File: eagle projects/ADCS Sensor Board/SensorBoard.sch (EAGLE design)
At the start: 88 parts, among them J5 HDR_10_EZFET_DEBUGGER, J6 MTI-1_8428-11B1-RK-TP, Q1 BC850SMD, Q2 IRF7507TRPBF, U1 MSP430F5529IPN, U2 LMV321, U3 ADS7841E_2K5, U4 LMV321, U5 LM20BIM7X_NOPB, U6 LMV321, Y1 32.768kHz, Y2 CSTCR4M00G15L99

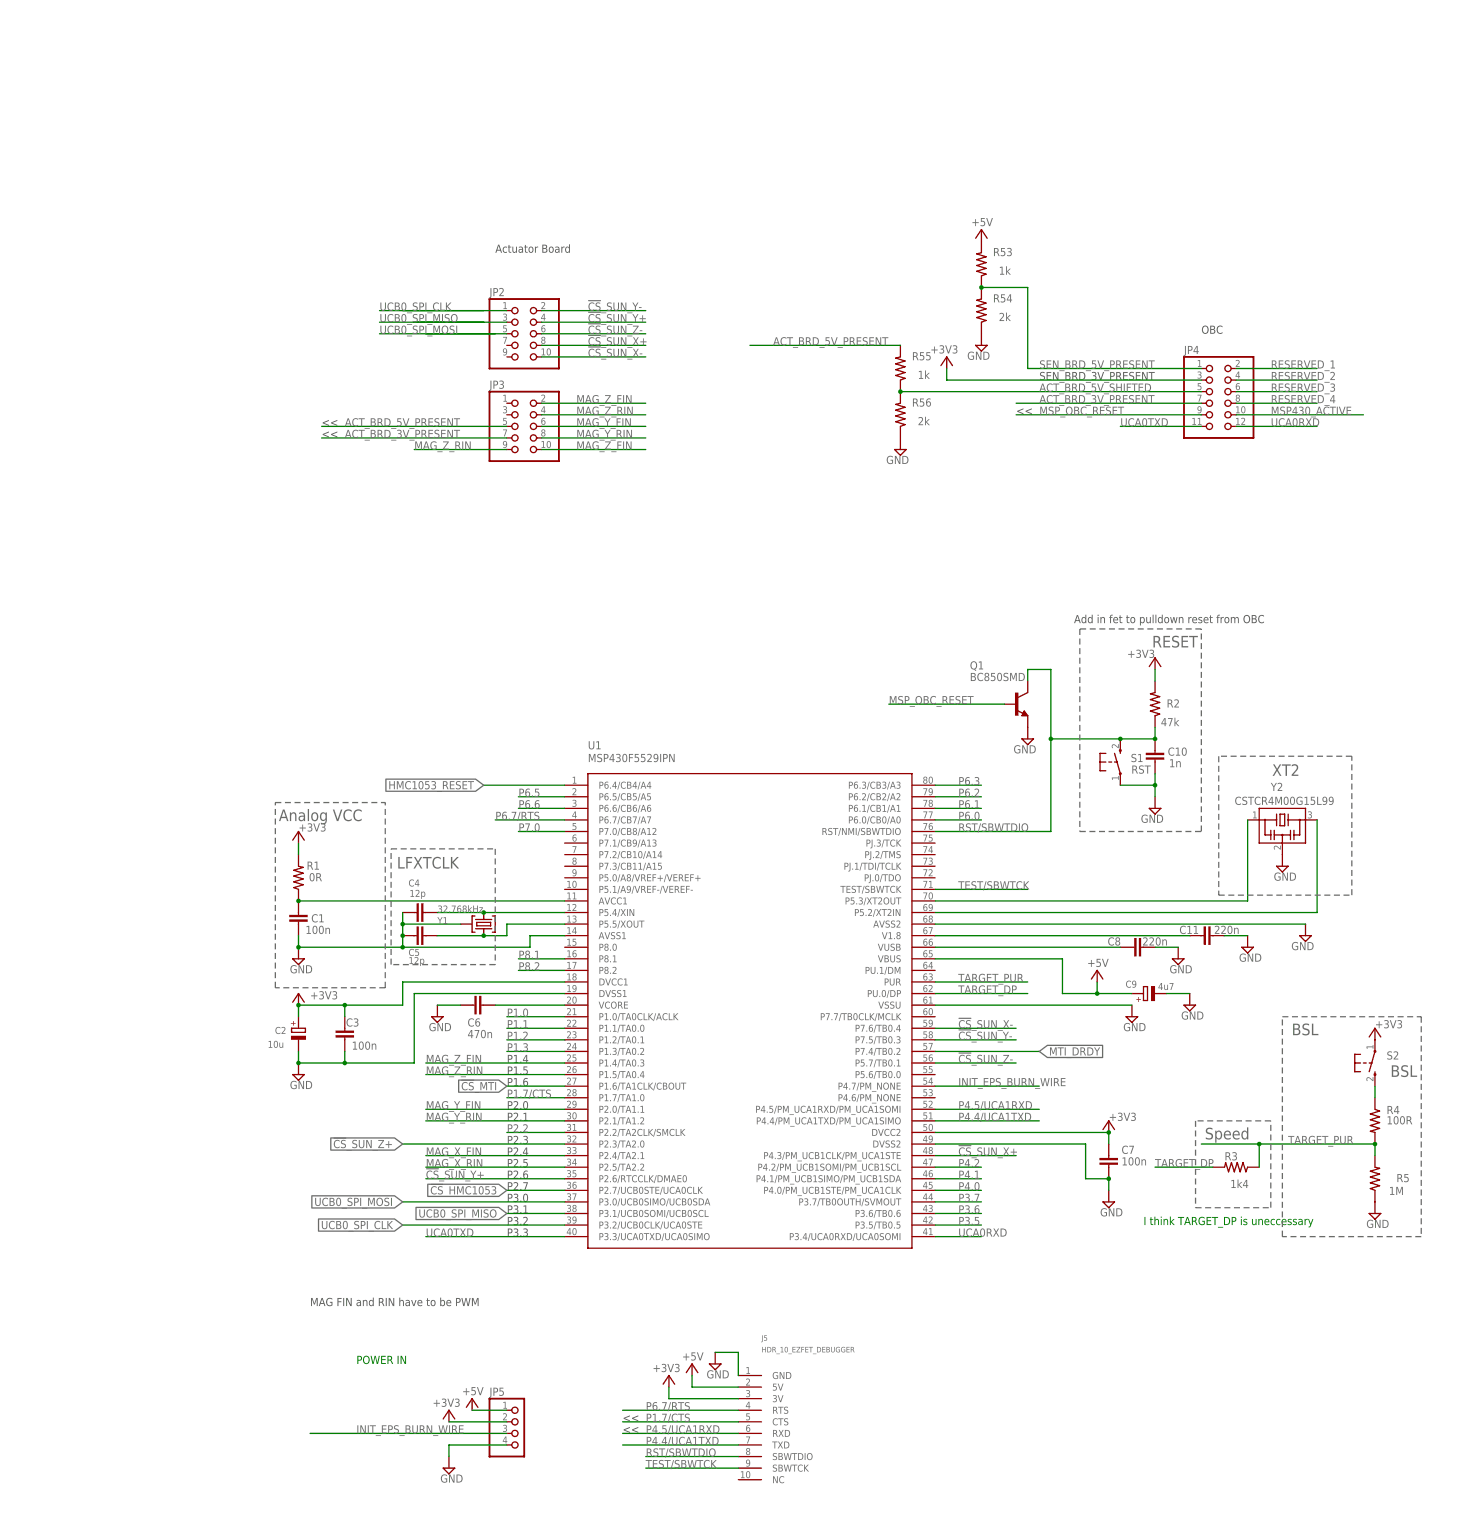
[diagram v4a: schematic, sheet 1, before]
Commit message: removed unused usb stuff from msp430
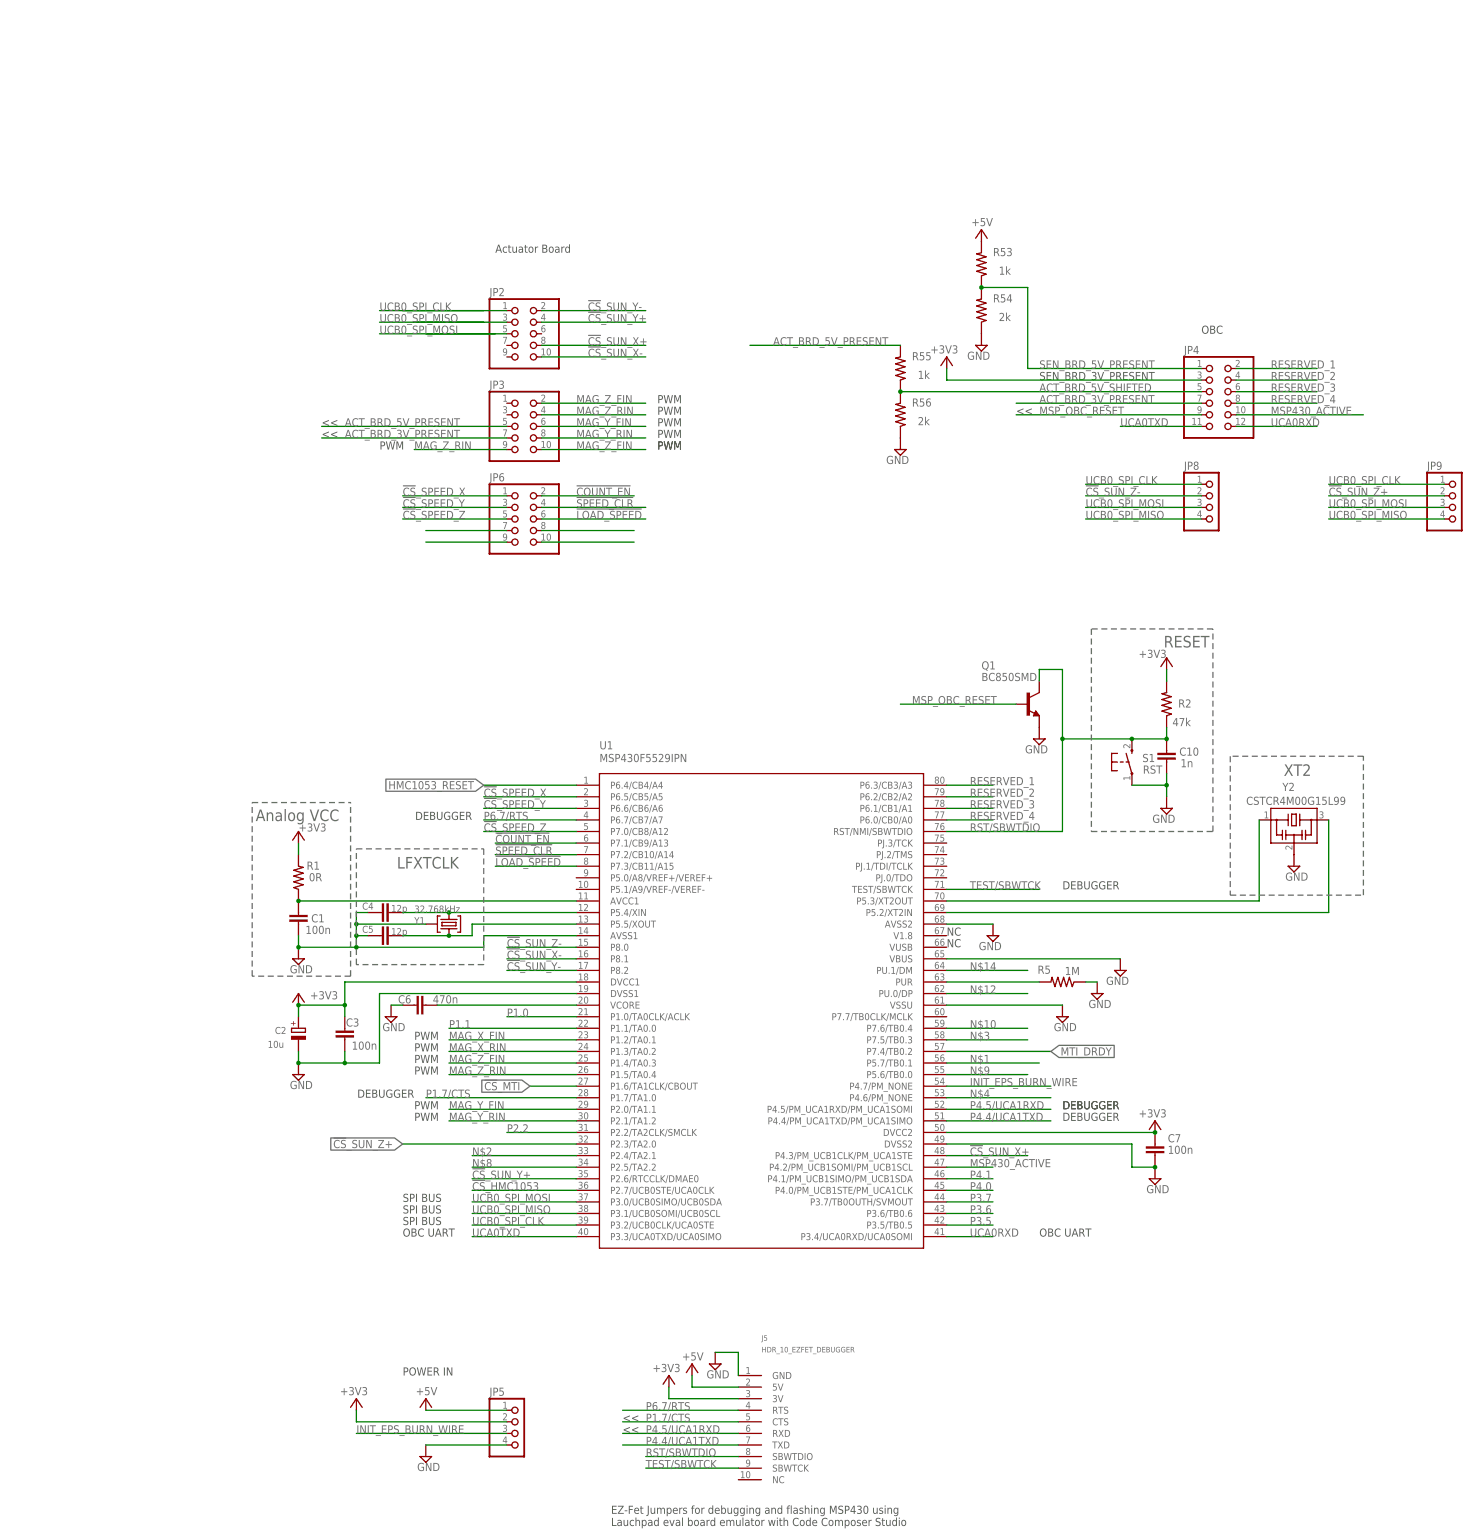
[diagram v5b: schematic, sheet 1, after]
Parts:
- removed C11, C8: 220n, rcl:C-EUC0402
- removed C9: 4u7, rcl:CPOL-EUA/3216-18R
- removed R3: 1k4, rcl:R-US_R0402
- removed R4: 100R, rcl:R-US_R0402
- removed S2: BSL, electricalmeter:PB
- added JP6: (no value), pinhead:PINHD-2X5
- added JP7: (no value), pinhead:PINHD-1X7
- added JP8, JP9: (no value), pinhead:PINHD-1X4
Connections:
- removed net N$17: A3.+5V
- removed net P1.2: U1.P1.2/TA0.1
- removed net P1.3: U1.P1.3/TA0.2
- removed net P4.2: U1.P4.2/PM_UCB1SOMI/PM_UCB1SCL
- removed net P6.0: U1.P6.0/CB0/A0
- removed net P6.1: U1.P6.1/CB1/A1
- removed net P6.2: U1.P6.2/CB2/A2
- removed net P6.3: U1.P6.3/CB3/A3
- removed net P6.5: U1.P6.5/CB5/A5
- removed net P6.6: U1.P6.6/CB6/A6
- removed net P7.0: U1.P7.0/CB8/A12
- removed net P8.1: U1.P8.1
- removed net P8.2: U1.P8.2
- removed net TARGET_DP: R3.2, U1.PU.0/DP
- removed net TARGET_VUSB1: C8.1, U1.VUSB
- removed net V1: C11.1, U1.V1.8
- new net !COUNT_EN: JP6.2, U1.P7.1/CB9/A13
- new net !CS!_SPEED_X: JP6.1, U1.P6.5/CB5/A5
- new net !CS!_SPEED_Y: JP6.3, U1.P6.6/CB6/A6
- new net !CS!_SPEED_Z: JP6.5, U1.P7.0/CB8/A12
- new net !LOAD_SPEED: JP6.6, U1.P7.3/CB11/A15
- new net !SPEED_CLR: JP6.4, U1.P7.2/CB10/A14
- new net N$10: U1.P7.6/TB0.4
- new net N$11: JP6.7
- new net N$13: JP6.9
- new net N$14: U1.PU.1/DM
- new net N$2: U1.P2.4/TA2.1
- new net N$3: U1.P7.5/TB0.3
- new net N$4: U1.P4.6/PM_NONE
- new net N$5: JP6.8
- new net N$6: JP6.10
- new net N$8: U1.P2.5/TA2.2
- new net N$9: U1.P5.6/TB0.0
- net !CS!_CAM_A: now also JP7.1
- net !CS!_CAM_B: now also JP7.2
- net !CS!_SUN_X-: now also U1.P8.1; no longer U1.P7.6/TB0.4
- net !CS!_SUN_Y-: now also U1.P8.2; no longer U1.P7.5/TB0.3
- net !CS!_SUN_Z+: now also JP9.2
- net !CS!_SUN_Z-: now also JP8.2, U1.P8.0; no longer JP2.6, U1.P5.7/TB0.1
- net +3V3: no longer S2.P
- net +5V: now also A3.+5V; no longer C9.+, U1.VBUS
- net GND: now also U1.VBUS; no longer C11.2, C8.2, C9.-
- net MAG_X_FIN: now also U1.P1.2/TA0.1; no longer U1.P2.4/TA2.1
- net MAG_X_RIN: now also U1.P1.3/TA0.2; no longer U1.P2.5/TA2.2
- net MSP430_ACTIVE: now also U1.P4.2/PM_UCB1SOMI/PM_UCB1SCL
- net MSP_OBC_RESET: now also Q1.B
- net N$1: now also U1.P5.7/TB0.1; no longer Q1.B
- net N$12: now also U1.PU.0/DP; no longer R4.1, S2.S
- net PAYLOAD_MISO: now also JP7.4
- net PAYLOAD_MOSI: now also JP7.3
- net PAYLOAD_SCL: now also JP7.7
- net PAYLOAD_SCLK: now also JP7.5
- net PAYLOAD_SDA: now also JP7.6
- net RESERVED_1: now also U1.P6.3/CB3/A3
- net RESERVED_2: now also U1.P6.2/CB2/A2
- net RESERVED_3: now also U1.P6.1/CB1/A1
- net RESERVED_4: now also U1.P6.0/CB0/A0
- net TARGET_PUR: no longer R3.1, R4.2
- net UCB0_SPI_CLK: now also JP8.1, JP9.1
- net UCB0_SPI_MISO: now also JP8.4, JP9.4
- net UCB0_SPI_MOSI: now also JP8.3, JP9.3
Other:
- note added: "DEBUGGER"
- note added: "EZ-Fet Jumpers for debugging and flashing MSP430 using Lauchpad eval board emulator with Code Composer Studio"
- note added: "NC"
- note added: "OBC UART"
- note added: "PWM"
- note added: "SPI BUS"
- note removed: "Add in fet to pulldown reset from OBC"
- note removed: "BSL"
- note removed: "I think TARGET_DP is uneccessary"
- note removed: "MAG FIN and RIN have to be PWM"
- note removed: "P1.4"
- note removed: "P1.5"
- note removed: "P1.6"
- note removed: "P2.0"
- note removed: "P2.1"
- note removed: "P2.3"
- note removed: "P2.4"
- note removed: "P2.5"
- note removed: "P2.6"
- note removed: "P2.7"
- note removed: "P3.0"
- note removed: "P3.1"
- note removed: "P3.2"
- note removed: "P3.3"
- note removed: "Speed"
- moved on the sheet: C10, C4, C5, C6, C7, Q1, R2, R5, S1, U1, Y1, Y2

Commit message: Finished up pinout connectors on sensor board
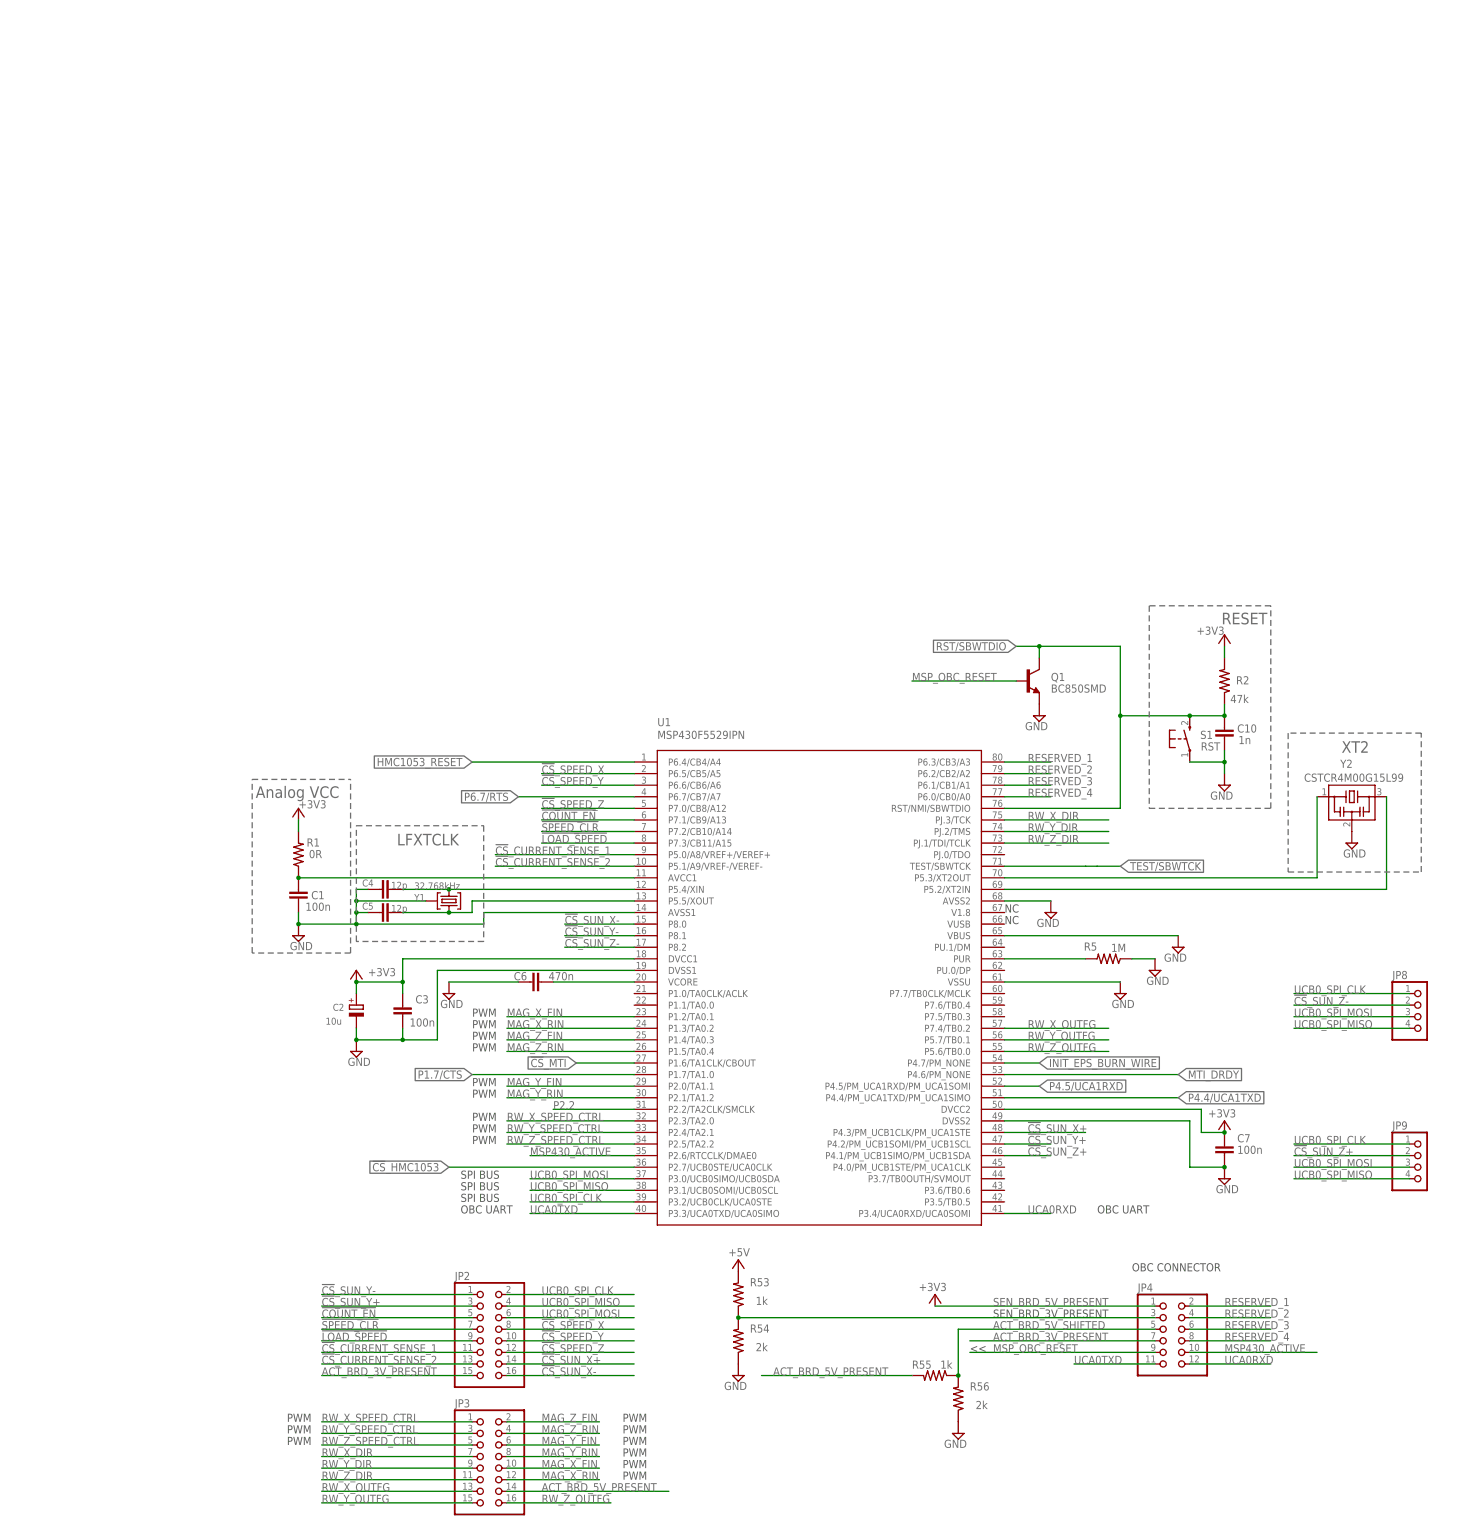
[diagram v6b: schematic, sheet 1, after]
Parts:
- removed JP6: (no value), pinhead:PINHD-2X5
- JP2, JP3: device pinhead:PINHD-2X5 -> pinhead:PINHD-2X8
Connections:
- removed net N$1: U1.P5.7/TB0.1
- removed net N$10: U1.P7.6/TB0.4
- removed net N$11: JP6.7
- removed net N$12: U1.PU.0/DP
- removed net N$13: JP6.9
- removed net N$14: U1.PU.1/DM
- removed net N$2: U1.P2.4/TA2.1
- removed net N$3: U1.P7.5/TB0.3
- removed net N$4: U1.P4.6/PM_NONE
- removed net N$5: JP6.8
- removed net N$6: JP6.10
- removed net N$8: U1.P2.5/TA2.2
- removed net N$9: U1.P5.6/TB0.0
- removed net P1.0: U1.P1.0/TA0CLK/ACLK
- removed net P1.1: U1.P1.1/TA0.0
- removed net P3.5: U1.P3.5/TB0.5
- removed net P3.6: U1.P3.6/TB0.6
- removed net P3.7: U1.P3.7/TB0OUTH/SVMOUT
- removed net P4.0: U1.P4.0/PM_UCB1STE/PM_UCA1CLK
- removed net P4.1: U1.P4.1/PM_UCB1SIMO/PM_UCB1SDA
- new net !CS!_CURRENT_SENSE_1: JP2.11, U1.P5.0/A8/VREF+/VEREF+
- new net !CS!_CURRENT_SENSE_2: JP2.13, U1.P5.1/A9/VREF-/VEREF-
- new net RW_X_DIR: JP3.7, U1.PJ.3/TCK
- new net RW_X_OUTFG: JP3.13, U1.P7.4/TB0.2
- new net RW_X_SPEED_CTRL: JP3.1, U1.P2.3/TA2.0
- new net RW_Y_DIR: JP3.9, U1.PJ.2/TMS
- new net RW_Y_OUTFG: JP3.15, U1.P5.7/TB0.1
- new net RW_Y_SPEED_CTRL: JP3.3, U1.P2.4/TA2.1
- new net RW_Z_DIR: JP3.11, U1.PJ.1/TDI/TCLK
- new net RW_Z_OUTFG: JP3.16, U1.P5.6/TB0.0
- new net RW_Z_SPEED_CTRL: JP3.5, U1.P2.5/TA2.2
- net !COUNT_EN: now also JP2.5; no longer JP6.2
- net !CS!_SPEED_X: now also JP2.8; no longer JP6.1
- net !CS!_SPEED_Y: now also JP2.10; no longer JP6.3
- net !CS!_SPEED_Z: now also JP2.12; no longer JP6.5
- net !CS!_SUN_X+: now also JP2.16; no longer JP2.10
- net !CS!_SUN_X-: now also JP2.14, U1.P8.0; no longer JP2.8, U1.P8.1
- net !CS!_SUN_Y+: now also JP2.3, U1.P4.2/PM_UCB1SOMI/PM_UCB1SCL; no longer JP2.4, U1.P2.6/RTCCLK/DMAE0
- net !CS!_SUN_Y-: now also JP2.1, U1.P8.1; no longer JP2.2, U1.P8.2
- net !CS!_SUN_Z+: now also U1.P4.1/PM_UCB1SIMO/PM_UCB1SDA; no longer U1.P2.3/TA2.0
- net !CS!_SUN_Z-: now also U1.P8.2; no longer U1.P8.0
- net !LOAD_SPEED: now also JP2.9; no longer JP6.6
- net !SPEED_CLR: now also JP2.7; no longer JP6.4
- net +3V3: now also JP4.1; no longer JP4.3
- net +5V: no longer J5.5V
- net ACT_BRD_3V_PRESENT: now also JP2.15; no longer JP3.7
- net ACT_BRD_5V_PRESENT: now also JP3.14; no longer JP3.5
- net MAG_X_FIN: now also JP3.10
- net MAG_X_RIN: now also JP3.12
- net MAG_Z_FIN: no longer JP3.10
- net MAG_Z_RIN: no longer JP3.9
- net MSP430_ACTIVE: now also U1.P2.6/RTCCLK/DMAE0; no longer U1.P4.2/PM_UCB1SOMI/PM_UCB1SCL
- net MTI_DRDY: now also U1.P4.6/PM_NONE; no longer U1.P7.4/TB0.2
- net SEN_BRD_5V_PRESENT: now also JP4.3; no longer JP4.1
- net UCB0_SPI_CLK: now also JP2.2; no longer JP2.1
- net UCB0_SPI_MISO: now also JP2.4; no longer JP2.3
- net UCB0_SPI_MOSI: now also JP2.6; no longer JP2.5
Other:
- note added: "OBC CONNECTOR"
- note removed: "Actuator Board"
- note removed: "DEBUGGER"
- note removed: "OBC"
- note removed: "POWER IN"
- moved on the sheet: C1, C10, C2, C3, C4, C5, C6, C7, JP4, JP7, JP8, JP9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
